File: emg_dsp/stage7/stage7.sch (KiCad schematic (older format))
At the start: 6 parts

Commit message: woooo working on the next microstimulator.
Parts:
- removed C?: 0.1uf, 0402, symbol C
- removed R?: 3k, symbol R
- removed U?: MCP4017, SC-70-6, symbol MCP4017
- added C10, C11, C12, C13, C14, C15, C16, C17, C2, C3, C4, C5, C6, C7, C8, C9: 0.1uf, 0402, symbol C
- added R1, R3, R4: 3k, 0402, symbol R
- added U1: 10X100, 11x100mil, symbol 10X100
- added U10, U11, U4, U5, U6, U7, U8, U9: IL715-3, SOIC-16, symbol ADUM2400
- added U3: 6533-CONN, SCSI68, symbol 6533-CONN
- R2: renamed from R?; footprint (none) -> 0402
- gave numbers to parts that had none: 2
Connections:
- net labels added: CGND, SCL, SDA, VEE, Vfb, a1, a2, a3, a4, a5, a6, a7, a8, an1, an10, an11, an12, an13, an14, an15, an2, an3, an4, an5, an6, an7, an8, an9, b1, b2, b3, b4, b5, b6, b7, b8, c1, c2, c3, c4, c5, c6, c7, c8, ca1, ca10, ca11, ca12, ca13, ca14, ca15, ca2, ca3, ca4, ca5, ca6, ca7, ca8, ca9, d1, d2, d3, d4, d5, d6, d7, d8
- net labels removed: AN1, AN2, AN3, AN4, AN5, AN6, AN7, AN8, CA1, CA2, CA3, CA4, CA5, CA6, CA7, CA8
- wire segments 18 -> 215
- no-connect marks 0 -> 13
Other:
- moved on the sheet: C1, U2

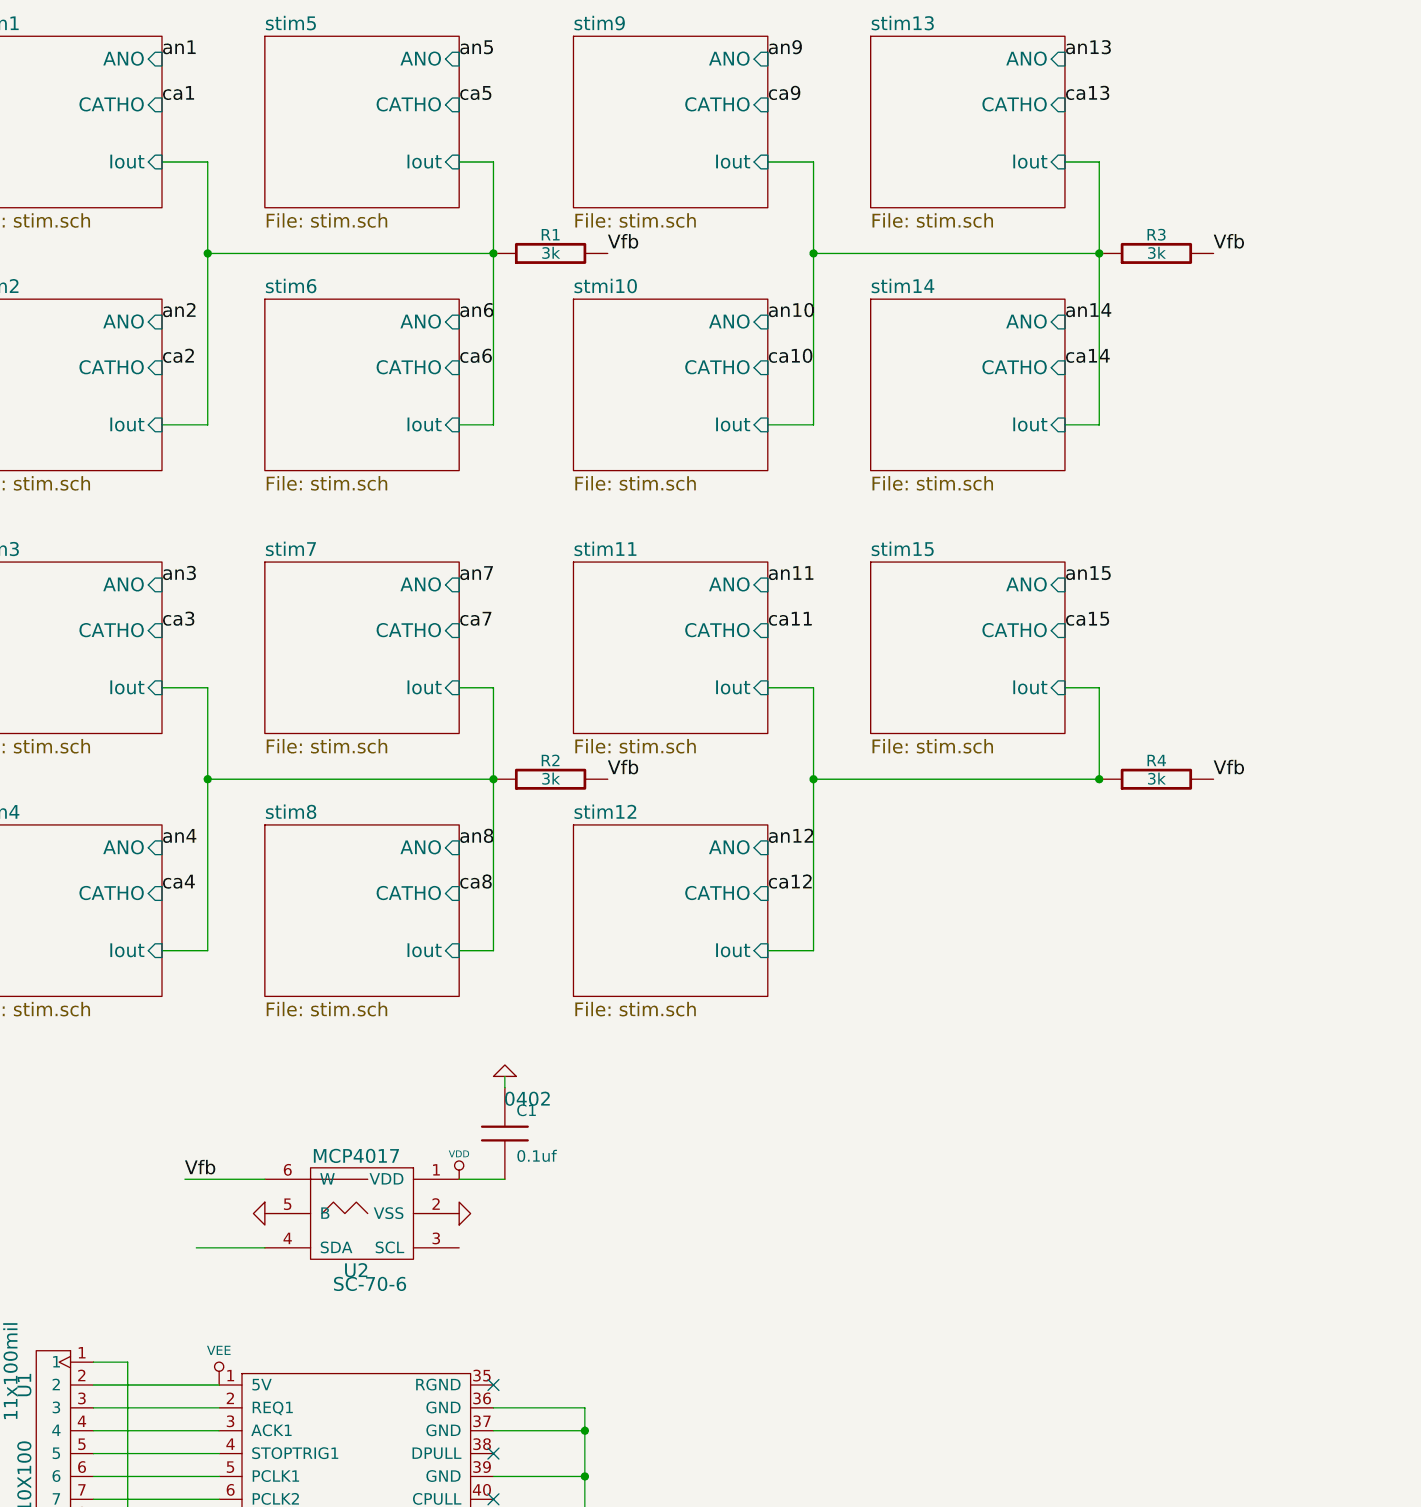
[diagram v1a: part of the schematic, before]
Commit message: wireless stimulator!
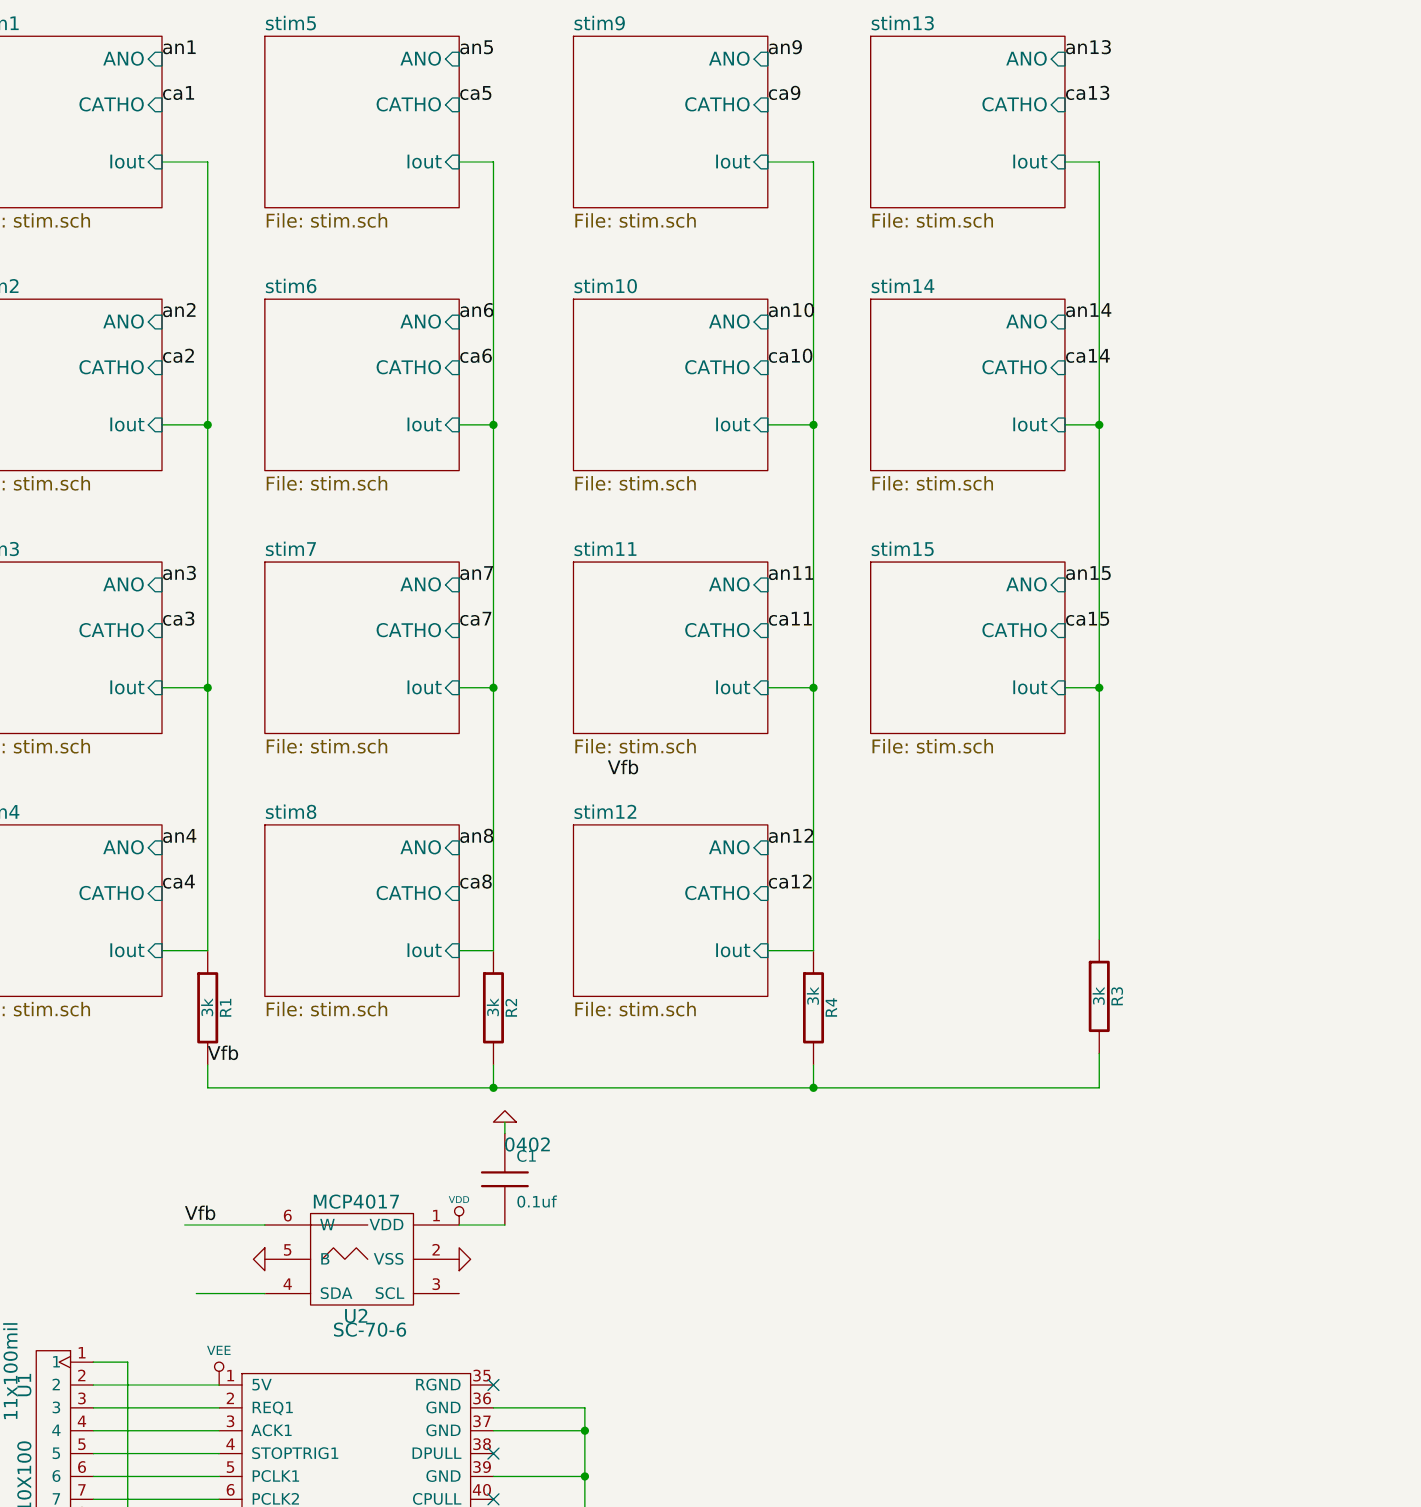
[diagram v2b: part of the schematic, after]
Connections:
- wire segments 215 -> 212
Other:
- moved on the sheet: C1, R1, R2, R3, R4, U2

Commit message: changed resistor value to 130ohm to decrease led brightness, changed vdd_OTP connection to regulator (MIC5365)
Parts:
- removed U1: 10X100, 11x100mil, symbol 10X100
- removed U10, U11, U4, U5, U6, U7, U8, U9: IL715-3, SOIC-16, symbol ADUM2400
- removed U2: MCP4017, SC-70-6, symbol MCP4017
- removed U3: 6533-CONN, SCSI68, symbol 6533-CONN
- added C18, C19, C27, C41, C42, C43: 10uf, 0603, symbol C
- added C20, C21, C22: 7pf, 0402, symbol C
- added C23, C25, C28, C32: 0.01uf, 0402, symbol C
- added C24, C248, C26, C29, C33, C34, C35, C36, C40, C47, C49, C50, C51, C52: 0.1uf, 0402, symbol C
- added C30, C37, C38, C39, C45, C48: 1uf, 0402, symbol C
- added C? (x2): 2.2uf, 0402, symbol C
- added D1, D10, D11, D12, D13, D14, D15, D16, D2, D3, D4, D5, D6, D7, D8, D9: LED, 0603, symbol LED
- added L1, L2: 2.2uh, 1210, symbol INDUCTOR
- added L3, L4: ferrite, 0402, symbol INDUCTOR
- added R10, R11, R12, R9: 22k, 0402, symbol R
- added R13, R14, R16, R38, R7: 33, 0402, symbol R
- added R15, R17, R26, R27, R28, R41: 10k, 0402, symbol R
- added R18, R19, R20, R21, R22, R23, R24, R25, R29, R30, R36, R37, R8: 50k, 0402, symbol R
- added R31: 12.1k, 0402, symbol R
- added R32, R33, R34, R35: 49.9, 0402, symbol R
- added R39, R40: 200, 0402, symbol R
- added R42, R43, R44, R45, R46, R47, R48, R49, R50, R51, R52, R53, R54, R55, R57: 50, 0402, symbol R
- added R5, R6: 90k, 0402, symbol R
- added R56: 130, 0402, symbol R
- added TP1: TWI_SCL, TP, symbol TP
- added TP10: NRF_IRQ, TP, symbol TP
- added TP11: WIRED_STEP, TP, symbol TP
- added TP12: PF0_DR0PRI, TP, symbol TP
- added TP13: PF1_RFS0, TP, symbol TP
- added TP14: PF2_RSCLK0, TP, symbol TP
- added TP15: PF3_DT0PRI, TP, symbol TP
- added TP16: PF4_TFS0, TP, symbol TP
- added TP17: PF5_TSCLK0, TP, symbol TP
- added TP18: PF6_DT0SEC, TP, symbol TP
- added TP19: PF7_DR0SEC, TP, symbol TP
- added TP2: TWI_SDA, TP, symbol TP
- added TP4: MOSI, TP, symbol TP
- added TP5: MISO, TP, symbol TP
- added TP6: SCK, TP, symbol TP
- added TP64, TP65, TP66, TP67: TP, 2.9mm_hole, symbol TP
- added TP7: SPISS, TP, symbol TP
- added TP8: NRF_CSN, TP, symbol TP
- added TP9: NRF_CE, TP, symbol TP
- added U1: RS232_CON, DB9, symbol RS232_CON
- added U10: EN_VDD, 2x100mil, symbol JUMP
- added U11: USBLC6, SOT-23-6, symbol USBLC6
- added U12: ABM10XTAL-24, ABM10, symbol ABM10XTAL
- added U13: BF527, MBGA-208, symbol BF527
- added U14: AT25DF041-MHF, SOIC-8, symbol AT25DF041-MHF
- added U15: ADSP_JTAG_CON, 7x2x100, symbol ADSP_JTAG_CON
- added U16: LAN8710A, QFN-32, symbol LAN8710A
- added U17, U22, U23: 74LCX541, TSSOP-20, symbol 74LCX541
- added U18: SFE-MAGJACK, SFE-MAGJACK, symbol SFE-MAGJACK
- added U19: NRF24L01-BREAK, 8x100mil, symbol NRF24L01-BREAK
- added U2: VEE, 2x100mil, symbol JUMP
- added U20: MAX6711Z, SC-70-4, symbol MAX6711
- added U21: TESTCON, 7x100mil, symbol TESTCON
- added U3: ADM3202, TSSOP-16, symbol ADM3202
- added U4: TPS62410, QFN-10, symbol TPS62410
- added U5: GT12MABE, GT12MABE, symbol GT12MABE
- added U6: FCI_USB_B, FCI_USB_B, symbol FCI_USB_B
- added U7: MT48LC16M16A2, VFBGA-54, symbol MT48LC16M16A2
- added U8: EN_VCC, 2x100mil, symbol JUMP
- added U9: ABM10XTAL-25, ABM10, symbol ABM10XTAL
- added U?: MIC5365, SC-70-5, symbol MIC5365
- C1: value 0.1uf -> 150uf; footprint 0402 -> 2917
- C15: value 0.1uf -> 7pf
- C16: value 0.1uf -> 33pf
- C17, C4, C5, C6: value 0.1uf -> 1uf
- C3: value 0.1uf -> 10uf; footprint 0402 -> 0603
- R1, R2: value 3k -> 33
- R3: value 3k -> 180k
- R4: value 3k -> 810k
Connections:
- net labels added: CLKBUF, COL, CRS, DATA0, DATA1, DATA10, DATA11, DATA12, DATA13, DATA14, DATA15, DATA2, DATA3, DATA4, DATA5, DATA6, DATA7, DATA8, DATA9, EVCC, EVDD, MDC, MDIO, MISO, MOSI, NRF_CE, NRF_CSN, NRF_IRQ, PF0, PF1, PF2, PF3, PF4, PF5, PF6, PF7, PG0, PHYINT, RESET, RX, RXCLK, RXD0, RXD1, RXD2, RXD3, RXDV, RXER, SCAS, SCK, SMS, SPISS, SRAS, SWE, TCK, TDI, TDO, TMS, TX, TXCLK, TXD0, TXD1, TXD2, TXD3, TXEN, VCC, WIRED_RESET, WIRED_STEP, _emu, _trst
- net labels removed: CGND, SCL, SDA, Vfb, a1, a2, a3, a4, a5, a6, a7, a8, an1, an10, an11, an12, an13, an14, an15, an2, an3, an4, an5, an6, an7, an8, an9, b1, b2, b3, b4, b5, b6, b7, b8, c1, c2, c3, c4, c5, c6, c7, c8, ca1, ca10, ca11, ca12, ca13, ca14, ca15, ca2, ca3, ca4, ca5, ca6, ca7, ca8, ca9, d1, d2, d3, d4, d5, d6, d7, d8
- wire segments 212 -> 521
- no-connect marks 13 -> 30
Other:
- note added: "1.2V"
- note added: "24MHz"
- note added: "25MHz"
- note added: "3.3V"
- note added: "I guess this really depends on how many I can fit"
- note added: "SPISS=SPISEL1"
- note added: "TPS62420 also ok"
- note added: "pinout for straight-through cable."
- note added: "power good!"
- note added: "the blackfin does not have 5v tolerant inputs"

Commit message: changed resistor values, added 4 caps
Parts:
- added C? (x2): 1uf, 0402, symbol C
- added C? (x6): 15pf, 0402, symbol C
- added R? (x2): 33, 0402, symbol R
- added R? (x2): 50k, 0402, symbol R
- added U? (x2): NRF24L01-BREAK, 8x100mil, symbol NRF24L01-BREAK
- R42, R43, R44, R45, R46, R47, R48, R49, R50, R51, R52, R53, R54, R55, R57: value 50 -> 130
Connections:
- net GND: now also C?.1, C?.1, C?.1, C?.1, C?.1, C?.1, C?.1, C?.1, U?.8 (GND), U?.8 (GND)
- net MISO: now also R?.1, R?.1
- net MOSI: now also C?.2, C?.2, C?.2, U?.5 (MOSI), U?.5 (MOSI)
- net NRF_CE: now also U?.2 (CE), U?.2 (CE)
- net NRF_CSN: no longer R37.2, U19.3 (CSN)
- net NRF_IRQ: no longer U19.7 (IRQ)
- net SCK: now also C?.2, C?.2, C?.2, U?.4 (SCK), U?.4 (SCK)
- net VDD: now also R?.1, R?.1
- net VEE: now also C?.2, C?.2, U?.1 (VCC), U?.1 (VCC)
- new net: R?.2, U?.6 (MISO) (x2)
- new net NRF_CSN0: R37.2, U19.3 (CSN)
- new net NRF_CSN1: R?.2, U?.3 (CSN)
- new net NRF_CSN2: R?.2, U?.3 (CSN)
- new net NRF_IRQ0: U19.7 (IRQ)
- new net NRF_IRQ1: U?.7 (IRQ)
- new net NRF_IRQ2: U?.7 (IRQ)
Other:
- moved on the sheet: C48, R36, R37, R38, U19

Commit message: adding changes to new board -- still feel that the schematic needs to be checked over, though.
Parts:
- gave numbers to parts that had none: 17
- renumbered C12 to C11, C11 to C12, C248 to C13, C13 to C14, C14 to C15, C15 to C16, C16 to C17, C17 to C18, C18 to C19, C19 to C20, C20 to C21, C21 to C22, C22 to C23, C23 to C25, C24 to C26, C25 to C27, C26 to C28, C27 to C29, C4 to C3, C28 to C30, C29 to C31, C30 to C32, C35 to C33, C32 to C35, C33 to C36, C34 to C37, C36 to C38, C37 to C39, C3 to C4, C38 to C40, C39 to C41, C40 to C42, C41 to C43, C42 to C44, C43 to C45, C47 to C46, C45 to C47, C49 to C48, C50 to C49, C51 to C53, C52 to C54, C48 to C58, C7 to C6, C6 to C7, C9 to C8, C8 to C9, R39 to R36, R40 to R37, R41 to R38, R36 to R39, R37 to R40, R38 to R41, R42 to R46, R43 to R47, R44 to R48, R45 to R49, R46 to R50, R47 to R51, R48 to R52, R49 to R53, R50 to R54, R51 to R55, R52 to R56, R53 to R57, R54 to R58, R55 to R59, R56 to R60, R57 to R61, TP64 to TP1, TP7 to TP10, TP8 to TP11, TP9 to TP12, TP10 to TP13, TP11 to TP14, TP12 to TP15, TP13 to TP16, TP14 to TP17, TP15 to TP18, TP16 to TP19, TP65 to TP2, TP17 to TP20, TP18 to TP21, TP19 to TP22, TP66 to TP3, TP67 to TP4, TP1 to TP5, TP2 to TP6, TP4 to TP7, TP5 to TP8, TP6 to TP9, U14 to U15, U15 to U16, U16 to U17, U17 to U18, U18 to U19, U19 to U24
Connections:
- net NRF_CE: now also U13.B3 (PF10-RFS1); no longer U13.K2 (PG10-TACI6), U22.7 (A6)
- net NRF_CSN0: now also U13.D2 (PF4-TFS0), U23.3 (A2)
- net NRF_CSN1: now also U13.C2 (PF6-DT0SEC), U23.5 (A4)
- net NRF_CSN2: now also U13.A2 (PF9-RSCLK1), U23.7 (A6)
- net NRF_IRQ0: now also U13.D1 (PF3-DT0PRI), U23.2 (A1)
- net NRF_IRQ1: now also U13.C1 (PF5-TSCLK0), U23.4 (A3)
- net NRF_IRQ2: now also U13.B2 (PF8-DR1PRI), U23.6 (A5)
- net PF15: now reaches U13.A6 (PF15-DR1SEC)
- net PF15: now also U23.9 (A8)
- net PF14: now reaches U13.B6 (PF14-DT1SEC)
- net PF14: now also U23.8 (A7)
- net NRF_CSN: no longer names the net of U13.K1 (PG9-TACI5)
- net NRF_CSN: no longer U22.6 (A5)
- net NRF_IRQ: no longer names the net of U13.J1 (PG11)
- net NRF_IRQ: no longer U22.8 (A7)
- net PF0 renamed DR0PRI
- net DR0PRI: now also U22.6 (A5); no longer U23.2 (A1)
- net PF1 renamed RFS0
- net RFS0: now also U22.8 (A7); no longer U23.3 (A2)
- net PF2 renamed RSCLK0
- net RSCLK0: now also U22.9 (A8); no longer U23.4 (A3)
- removed net PF3: U13.D1 (PF3-DT0PRI), U23.5 (A4)
- removed net PF4: U13.D2 (PF4-TFS0), U23.6 (A5)
- removed net PF5: U13.C1 (PF5-TSCLK0), U23.7 (A6)
- removed net PF6: U13.C2 (PF6-DT0SEC), U23.8 (A7)
- net PF7 renamed DR0SEC
- net DR0SEC: now also U22.7 (A6); no longer U23.9 (A8)
- net WIRED_RESET: no longer names the net of U13.M2 (PG6-TMR2)
- net WIRED_STEP: no longer names the net of U13.M1 (PG5-TMR1)
- net WIRED_STEP: no longer U22.9 (A8)
- no-connect marks 30 -> 25

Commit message: schematic improvements / modifications.
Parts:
- added C?: 100pf, 0402, symbol C
- added C?: 0.1uf, 0402, symbol C
- added R? (x11): 130, 0402, symbol R
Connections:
- net DR0PRI: now also R?.2; no longer U22.6 (A5)
- net DR0SEC: now also R?.2; no longer U22.7 (A6)
- net GND: now also C?.2, C?.2
- net MISO: now also R?.1, R?.2; no longer U18.5 (A4), U22.3 (A2)
- net MOSI: now also R?.2, R?.2; no longer U18.17 (Y2), U22.2 (A1)
- net RFS0: now also R?.2; no longer U22.8 (A7)
- net RSCLK0: now also R?.2; no longer U22.9 (A8)
- net SCK: now also R?.2, R?.2; no longer U18.16 (Y3), U22.4 (A3)
- net SPISS: now also R?.2; no longer U22.5 (A4)
- net VCC: now also C?.1
- net at U18.4 (A3), U21.6 (SCK): now also C?.1
- new net: R?.1, U18.16 (Y3)
- new net: R?.1, U18.17 (Y2)
- new net: R?.2, U18.5 (A4)
- new net: R?.1, U22.2 (A1)
- new net: R?.1, U22.3 (A2)
- new net: R?.1, U22.4 (A3)
- new net: R?.1, U22.5 (A4)
- new net: R?.1, U22.6 (A5)
- new net: R?.1, U22.7 (A6)
- new net: R?.1, U22.8 (A7)
- new net: R?.1, U22.9 (A8)
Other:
- moved on the sheet: C49

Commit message: starting placement of modules in board...
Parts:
- gave numbers to parts that had none: 13
- renumbered C46 to C47, C47 to C48, C48 to C49, C49 to C50, C50 to C52, C51 to C53, C52 to C54, C53 to C55, C54 to C56, C55 to C57, C56 to C58, C57 to C59, C58 to C60, C59 to C61, C60 to C62, R36 to R38, R37 to R39, R38 to R41, R39 to R50, R40 to R51, R41 to R52, R42 to R53, R43 to R54, R44 to R55, R45 to R56, R46 to R57, R47 to R58, R48 to R59, R49 to R60, R50 to R61, R51 to R62, R52 to R63, R53 to R64, R54 to R65, R55 to R66, R56 to R67, R57 to R68, R58 to R69, R59 to R70, R60 to R71, R61 to R72
